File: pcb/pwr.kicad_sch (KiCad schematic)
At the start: 20 parts, among them J2 39-29-3086

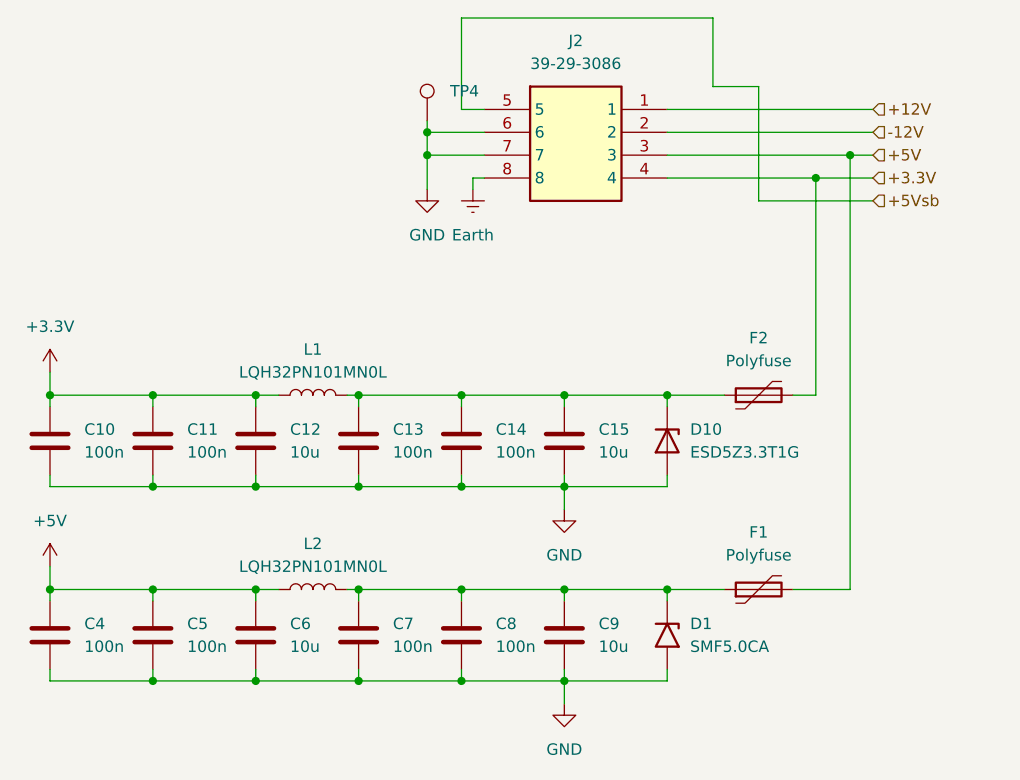
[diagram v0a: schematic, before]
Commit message: Sch complete, starting pcb
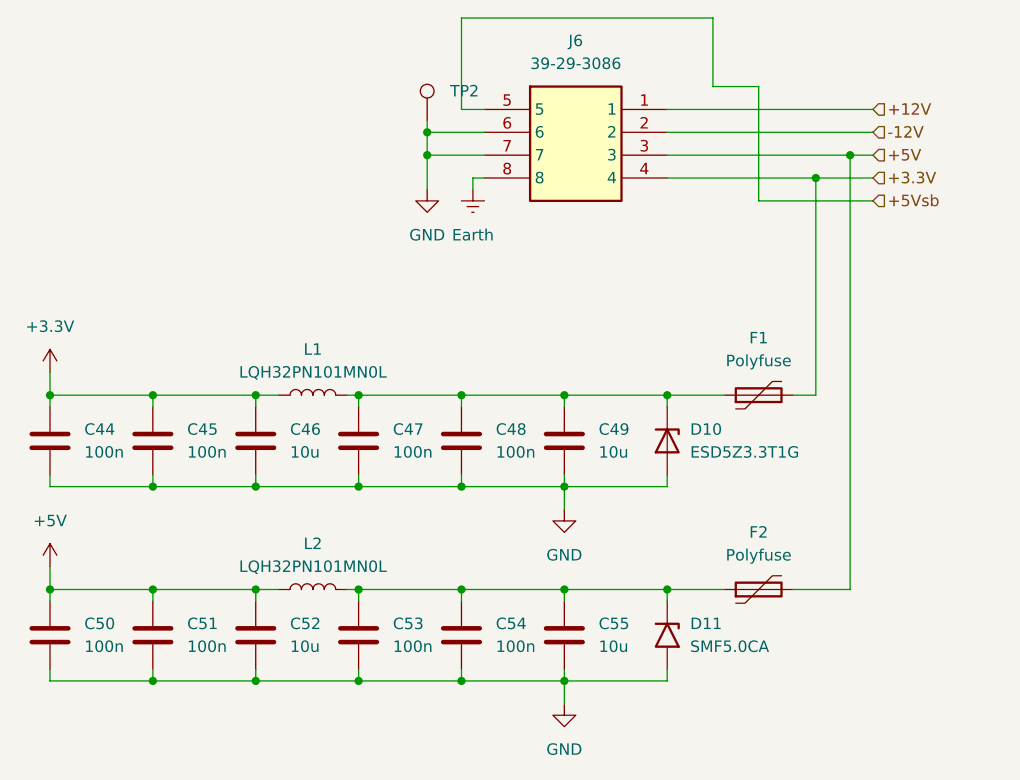
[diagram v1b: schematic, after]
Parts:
- renumbered C10 to C44, C11 to C45, C12 to C46, C13 to C47, C14 to C48, C15 to C49, C4 to C50, C5 to C51, C6 to C52, C7 to C53, C8 to C54, C9 to C55, D1 to D11, F2 to F1, F1 to F2, J2 to J6, TP4 to TP2
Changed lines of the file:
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@@
 		(dnp no)
 		(fields_autoplaced yes)
-		(property "Reference" "#PWR03"
+		(property "Reference" "#PWR055"
 			(at 142.24 118.11 0)
 			(effects
@@
 			(project "QCB_board"
 				(path "/3a9957e4-3d4a-4c65-a0c0-c287bc2a56fb/f3b8231f-7b82-4f83-9deb-cd261a39bfe5"
-					(reference "#PWR03")
+					(reference "#PWR055")
 					(unit 1)
 				)
@@
 		(dnp no)
 		(fields_autoplaced yes)
-		(property "Reference" "C10"
+		(property "Reference" "C44"
 			(at 88.9 102.8699 0)
 			(effects
@@
 			(project "QCB_board"
 				(path "/3a9957e4-3d4a-4c65-a0c0-c287bc2a56fb/f3b8231f-7b82-4f83-9deb-cd261a39bfe5"
-					(reference "C10")
+					(reference "C44")
 					(unit 1)
 				)
@@
 		(dnp no)
 		(fields_autoplaced yes)
-		(property "Reference" "C12"
+		(property "Reference" "C46"
 			(at 111.76 102.8699 0)
 			(effects
@@
 			(project "QCB_board"
 				(path "/3a9957e4-3d4a-4c65-a0c0-c287bc2a56fb/f3b8231f-7b82-4f83-9deb-cd261a39bfe5"
-					(reference "C12")
+					(reference "C46")
 					(unit 1)
 				)
@@
 		(dnp no)
 		(fields_autoplaced yes)
-		(property "Reference" "#PWR07"
+		(property "Reference" "#PWR052"
 			(at 127 82.55 0)
 			(effects
@@
 			(project "QCB_board"
 				(path "/3a9957e4-3d4a-4c65-a0c0-c287bc2a56fb/f3b8231f-7b82-4f83-9deb-cd261a39bfe5"
-					(reference "#PWR07")
+					(reference "#PWR052")
 					(unit 1)
 				)
@@
 		(dnp no)
 		(fields_autoplaced yes)
-		(property "Reference" "F1"
+		(property "Reference" "F2"
 			(at 163.83 114.3 90)
 			(effects
@@
 			(project "QCB_board"
 				(path "/3a9957e4-3d4a-4c65-a0c0-c287bc2a56fb/f3b8231f-7b82-4f83-9deb-cd261a39bfe5"
-					(reference "F1")
+					(reference "F2")
 					(unit 1)
 				)
@@
 		(dnp no)
 		(fields_autoplaced yes)
-		(property "Reference" "D1"
+		(property "Reference" "D11"
 			(at 156.21 124.4599 90)
 			(effects
@@
 			(project "QCB_board"
 				(path "/3a9957e4-3d4a-4c65-a0c0-c287bc2a56fb/f3b8231f-7b82-4f83-9deb-cd261a39bfe5"
-					(reference "D1")
+					(reference "D11")
 					(unit 1)
 				)
@@
 		(dnp no)
 		(fields_autoplaced yes)
-		(property "Reference" "C13"
+		(property "Reference" "C47"
 			(at 123.19 102.8699 0)
 			(effects
@@
 			(project "QCB_board"
 				(path "/3a9957e4-3d4a-4c65-a0c0-c287bc2a56fb/f3b8231f-7b82-4f83-9deb-cd261a39bfe5"
-					(reference "C13")
+					(reference "C47")
 					(unit 1)
 				)
@@
 		(dnp no)
 		(fields_autoplaced yes)
-		(property "Reference" "#PWR08"
+		(property "Reference" "#PWR053"
 			(at 132.08 82.55 0)
 			(effects
@@
 			(project "QCB_board"
 				(path "/3a9957e4-3d4a-4c65-a0c0-c287bc2a56fb/f3b8231f-7b82-4f83-9deb-cd261a39bfe5"
-					(reference "#PWR08")
+					(reference "#PWR053")
 					(unit 1)
 				)
@@
 		(dnp no)
 		(fields_autoplaced yes)
-		(property "Reference" "#PWR02"
+		(property "Reference" "#PWR057"
 			(at 142.24 139.7 0)
 			(effects
@@
 			(project "QCB_board"
 				(path "/3a9957e4-3d4a-4c65-a0c0-c287bc2a56fb/f3b8231f-7b82-4f83-9deb-cd261a39bfe5"
-					(reference "#PWR02")
+					(reference "#PWR057")
 					(unit 1)
 				)
@@
 		(dnp no)
 		(fields_autoplaced yes)
-		(property "Reference" "#PWR027"
+		(property "Reference" "#PWR054"
 			(at 85.09 100.33 0)
 			(effects
@@
 			(project "QCB_board"
 				(path "/3a9957e4-3d4a-4c65-a0c0-c287bc2a56fb/f3b8231f-7b82-4f83-9deb-cd261a39bfe5"
-					(reference "#PWR027")
+					(reference "#PWR054")
 					(unit 1)
 				)
@@
 		(dnp no)
 		(fields_autoplaced yes)
-		(property "Reference" "J2"
+		(property "Reference" "J6"
 			(at 143.51 59.69 0)
 			(effects
@@
 			(project "QCB_board"
 				(path "/3a9957e4-3d4a-4c65-a0c0-c287bc2a56fb/f3b8231f-7b82-4f83-9deb-cd261a39bfe5"
-					(reference "J2")
+					(reference "J6")
 					(unit 1)
 				)
@@
 		(dnp no)
 		(fields_autoplaced yes)
-		(property "Reference" "C5"
+		(property "Reference" "C51"
 			(at 100.33 124.4599 0)
 			(effects
@@
 			(project "QCB_board"
 				(path "/3a9957e4-3d4a-4c65-a0c0-c287bc2a56fb/f3b8231f-7b82-4f83-9deb-cd261a39bfe5"
-					(reference "C5")
+					(reference "C51")
 					(unit 1)
 				)
@@
 		(dnp no)
 		(fields_autoplaced yes)
-		(property "Reference" "C4"
+		(property "Reference" "C50"
 			(at 88.9 124.4599 0)
 			(effects
@@
 			(project "QCB_board"
 				(path "/3a9957e4-3d4a-4c65-a0c0-c287bc2a56fb/f3b8231f-7b82-4f83-9deb-cd261a39bfe5"
-					(reference "C4")
+					(reference "C50")
 					(unit 1)
 				)
@@
 		(dnp no)
 		(fields_autoplaced yes)
-		(property "Reference" "F2"
+		(property "Reference" "F1"
 			(at 163.83 92.71 90)
 			(effects
@@
 			(project "QCB_board"
 				(path "/3a9957e4-3d4a-4c65-a0c0-c287bc2a56fb/f3b8231f-7b82-4f83-9deb-cd261a39bfe5"
-					(reference "F2")
+					(reference "F1")
 					(unit 1)
 				)
@@
 		(dnp no)
 		(fields_autoplaced yes)
-		(property "Reference" "C14"
+		(property "Reference" "C48"
 			(at 134.62 102.8699 0)
 			(effects
@@
 			(project "QCB_board"
 				(path "/3a9957e4-3d4a-4c65-a0c0-c287bc2a56fb/f3b8231f-7b82-4f83-9deb-cd261a39bfe5"
-					(reference "C14")
+					(reference "C48")
 					(unit 1)
 				)
@@
 		(dnp no)
 		(fields_autoplaced yes)
-		(property "Reference" "C8"
+		(property "Reference" "C54"
 			(at 134.62 124.4599 0)
 			(effects
@@
 			(project "QCB_board"
 				(path "/3a9957e4-3d4a-4c65-a0c0-c287bc2a56fb/f3b8231f-7b82-4f83-9deb-cd261a39bfe5"
-					(reference "C8")
+					(reference "C54")
 					(unit 1)
 				)
@@
 		(dnp no)
 		(fields_autoplaced yes)
-		(property "Reference" "C9"
+		(property "Reference" "C55"
 			(at 146.05 124.4599 0)
 			(effects
@@
 			(project "QCB_board"
 				(path "/3a9957e4-3d4a-4c65-a0c0-c287bc2a56fb/f3b8231f-7b82-4f83-9deb-cd261a39bfe5"
-					(reference "C9")
+					(reference "C55")
 					(unit 1)
 				)
@@
 		(dnp no)
 		(fields_autoplaced yes)
-		(property "Reference" "C11"
+		(property "Reference" "C45"
 			(at 100.33 102.8699 0)
 			(effects
@@
 			(project "QCB_board"
 				(path "/3a9957e4-3d4a-4c65-a0c0-c287bc2a56fb/f3b8231f-7b82-4f83-9deb-cd261a39bfe5"
-					(reference "C11")
+					(reference "C45")
 					(unit 1)
 				)
@@
 		(dnp no)
 		(fields_autoplaced yes)
-		(property "Reference" "C6"
+		(property "Reference" "C52"
 			(at 111.76 124.4599 0)
 			(effects
@@
 			(project "QCB_board"
 				(path "/3a9957e4-3d4a-4c65-a0c0-c287bc2a56fb/f3b8231f-7b82-4f83-9deb-cd261a39bfe5"
-					(reference "C6")
+					(reference "C52")
 					(unit 1)
 				)
@@
 		(dnp no)
 		(fields_autoplaced yes)
-		(property "Reference" "TP4"
+		(property "Reference" "TP2"
 			(at 129.54 65.2779 0)
 			(effects
@@
 			(project "QCB_board"
 				(path "/3a9957e4-3d4a-4c65-a0c0-c287bc2a56fb/f3b8231f-7b82-4f83-9deb-cd261a39bfe5"
-					(reference "TP4")
+					(reference "TP2")
 					(unit 1)
 				)
@@
 		(dnp no)
 		(fields_autoplaced yes)
-		(property "Reference" "C7"
+		(property "Reference" "C53"
 			(at 123.19 124.4599 0)
 			(effects
@@
 			(project "QCB_board"
 				(path "/3a9957e4-3d4a-4c65-a0c0-c287bc2a56fb/f3b8231f-7b82-4f83-9deb-cd261a39bfe5"
-					(reference "C7")
+					(reference "C53")
 					(unit 1)
 				)
@@
 		(dnp no)
 		(fields_autoplaced yes)
-		(property "Reference" "C15"
+		(property "Reference" "C49"
 			(at 146.05 102.8699 0)
 			(effects
@@
 			(project "QCB_board"
 				(path "/3a9957e4-3d4a-4c65-a0c0-c287bc2a56fb/f3b8231f-7b82-4f83-9deb-cd261a39bfe5"
-					(reference "C15")
+					(reference "C49")
 					(unit 1)
 				)
@@
 		(dnp no)
 		(fields_autoplaced yes)
-		(property "Reference" "#PWR04"
+		(property "Reference" "#PWR056"
 			(at 85.09 121.92 0)
 			(effects
@@
 			(project "QCB_board"
 				(path "/3a9957e4-3d4a-4c65-a0c0-c287bc2a56fb/f3b8231f-7b82-4f83-9deb-cd261a39bfe5"
-					(reference "#PWR04")
-					(unit 1)
-				)
+					(reference "#PWR056")
+					(unit 1)
+				)

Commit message: Routing
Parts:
- removed C50, C51, C53, C54: 100n, Capacitor_SMD:C_0603_1608Metric_Pad1.08x0.95mm_HandSolder, symbol Device:C
- removed C52, C55: 10u, Capacitor_SMD:C_1206_3216Metric_Pad1.33x1.80mm_HandSolder, symbol Device:C
- removed D11: SMF5.0CA, Diode_SMD:D_SMF, symbol Diode:SMF5V0A
- removed F2: Polyfuse, Fuse:Fuse_1206_3216Metric_Pad1.42x1.75mm_HandSolder, symbol Device:Polyfuse
- removed L2: LQH32PN101MN0L, Inductor_SMD:L_1210_3225Metric, symbol Device:L
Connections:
- net +3.3V: no longer F1.2, J6.4
- net +12V renamed +12V_PWR
- net +5V renamed +5V_PWR
- net -12V renamed -12V_PWR
- new net +3.3V_PWR: F1.2, J6.4
